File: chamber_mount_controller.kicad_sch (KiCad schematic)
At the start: 10 parts, among them J1 Conn_01x04, J2 Conn_01x04, J3 Conn_01x02, SW1 SW_DIP_x02, SW2 SW_DIP_x02, U1 MP6500, U2 MP6500

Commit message: updated files
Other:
- moved on the sheet: SW1
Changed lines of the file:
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@@
     (stroke (width 0) (type default) (color 0 0 0 0))
   )
-  (wire (pts (xy 179.07 66.04) (xy 181.61 66.04))
+  (wire (pts (xy 180.34 66.04) (xy 181.61 66.04))
     (stroke (width 0) (type default) (color 0 0 0 0))
   )
@@
     (stroke (width 0) (type default) (color 0 0 0 0))
   )
-  (wire (pts (xy 163.83 66.04) (xy 161.29 66.04))
+  (wire (pts (xy 165.1 66.04) (xy 161.29 66.04))
     (stroke (width 0) (type default) (color 0 0 0 0))
   )
@@
     (stroke (width 0) (type default) (color 0 0 0 0))
   )
-  (wire (pts (xy 161.29 63.5) (xy 163.83 63.5))
+  (wire (pts (xy 161.29 63.5) (xy 165.1 63.5))
     (stroke (width 0) (type default) (color 0 0 0 0))
   )
@@
     (stroke (width 0) (type default) (color 0 0 0 0))
   )
-  (wire (pts (xy 179.07 63.5) (xy 179.07 64.77))
+  (wire (pts (xy 180.34 63.5) (xy 180.34 64.77))
     (stroke (width 0) (type default) (color 0 0 0 0))
   )
@@
     (stroke (width 0) (type default) (color 0 0 0 0))
   )
-  (wire (pts (xy 179.07 64.77) (xy 182.88 64.77))
+  (wire (pts (xy 180.34 64.77) (xy 182.88 64.77))
     (stroke (width 0) (type default) (color 0 0 0 0))
   )
@@
     (pin "4")
   )
-  (symbol (lib_id "Switch:SW_DIP_x02") (at 171.45 66.04 0) (unit 1)
-    (in_bom yes) (on_board yes) (fields_autoplaced)
-    (property "Reference" "SW1" (id 0) (at 171.45 55.88 0))
-    (property "Value" "SW_DIP_x02" (id 1) (at 171.45 58.42 0))
-    (property "Footprint" "Package_DIP:DIP-4_W7.62mm" (id 2) (at 171.45 66.04 0)
-      (effects (font (size 1.27 1.27)) hide)
-    )
-    (property "Datasheet" "~" (id 3) (at 171.45 66.04 0)
-      (effects (font (size 1.27 1.27)) hide)
-    )
+  (symbol (lib_id "Switch:SW_DIP_x02") (at 172.72 66.04 0) (unit 1)
+    (in_bom yes) (on_board yes) (fields_autoplaced)
+    (property "Reference" "SW1" (id 0) (at 172.72 55.88 0))
+    (property "Value" "SW_DIP_x02" (id 1) (at 172.72 58.42 0))
+    (property "Footprint" "Package_DIP:DIP-4_W7.62mm" (id 2) (at 172.72 66.04 0)
+      (effects (font (size 1.27 1.27)) hide)
+    )
+    (property "Datasheet" "~" (id 3) (at 172.72 66.04 0)
+      (effects (font (size 1.27 1.27)) hide)
+    )

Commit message: Redid layout for arduino nano, added DC barrel jack
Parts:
- C1: footprint Capacitor_THT:CP_Radial_D5.0mm_P2.00mm -> Capacitor_THT:CP_Radial_D5.0mm_P2.50mm
- J3: footprint Connector_PinHeader_2.54mm:PinHeader_1x02_P2.54mm_Vertical -> Connector_BarrelJack:BarrelJack_CUI_PJ-063AH_Horizontal
- XA1: footprint Arduino:Arduino_Uno_Shield -> Module:Arduino_Nano; symbol arduino:Arduino_Uno_Shield -> MCU_Module:Arduino_Nano_Every
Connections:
- net +5V: now also XA1.27 (+5V); no longer XA1.5V1 (5V)
- net GND: now also XA1.29 (GND), XA1.4 (GND); no longer XA1.GND1 (GND), XA1.GND2 (GND), XA1.GND3 (GND)
- net at U1.8 (dir): now also XA1.10 (D7); no longer XA1.D6
- net at U1.7 (step): now also XA1.11 (D8); no longer XA1.D7
- net at U2.8 (dir): now also XA1.12 (D9); no longer XA1.D8
- net at U2.7 (step): now also XA1.13 (D10); no longer XA1.D9
- net at SW2.3: now also U2.3 (ms2); no longer U2.2 (ms1)
- net at SW2.4: now also U2.2 (ms1); no longer U2.3 (ms2)
- net at SW1.3: now also U1.3 (ms2); no longer U1.2 (ms1)
- net at SW1.4: now also U1.2 (ms1); no longer U1.3 (ms2)
- no-connect marks 36 -> 29

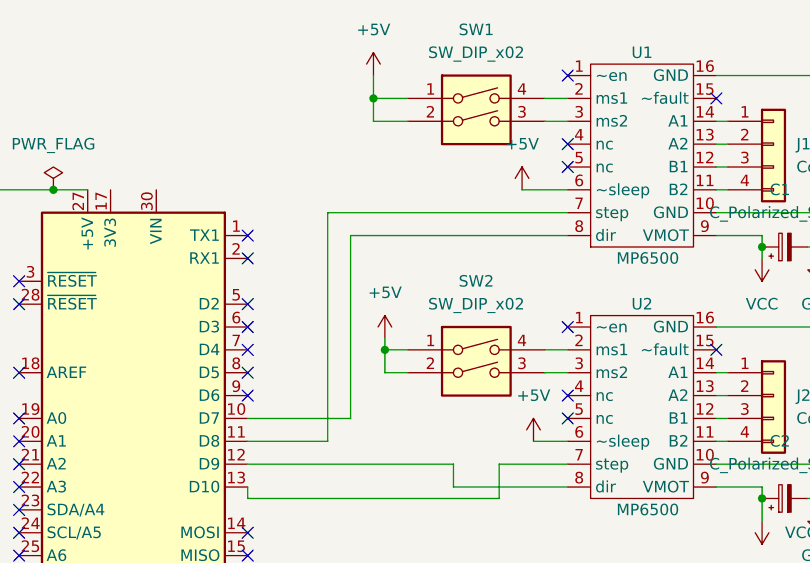
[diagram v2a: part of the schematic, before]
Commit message: Re-routed traces to remove need for microstepping DIP switches
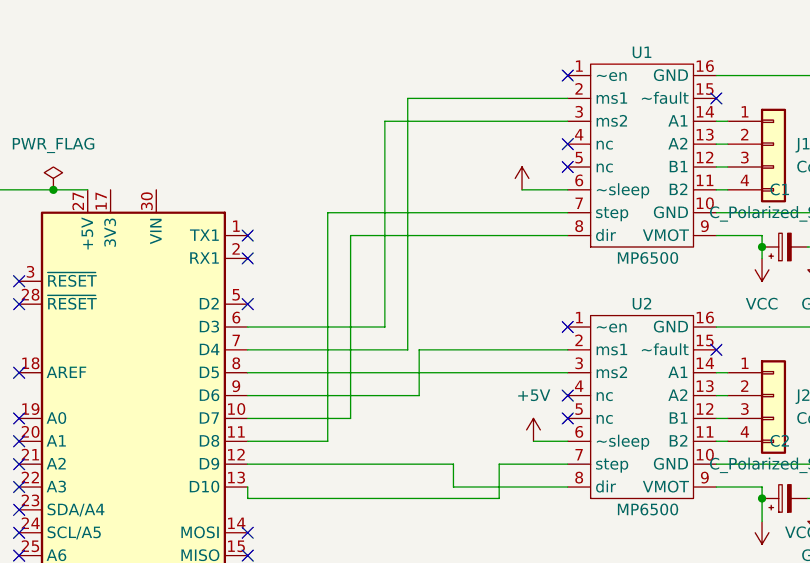
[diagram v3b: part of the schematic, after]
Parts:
- removed SW1, SW2: SW_DIP_x02, Package_DIP:DIP-4_W7.62mm, symbol Switch:SW_DIP_x02
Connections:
- net at XA1.6 (D3): now also U1.3 (ms2)
- net at XA1.7 (D4): now also U1.2 (ms1)
- net at XA1.8 (D5): now also U2.3 (ms2)
- net at XA1.9 (D6): now also U2.2 (ms1)
- no-connect marks 29 -> 25
